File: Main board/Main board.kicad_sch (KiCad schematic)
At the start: 41 parts, among them J1 Conn_01x03

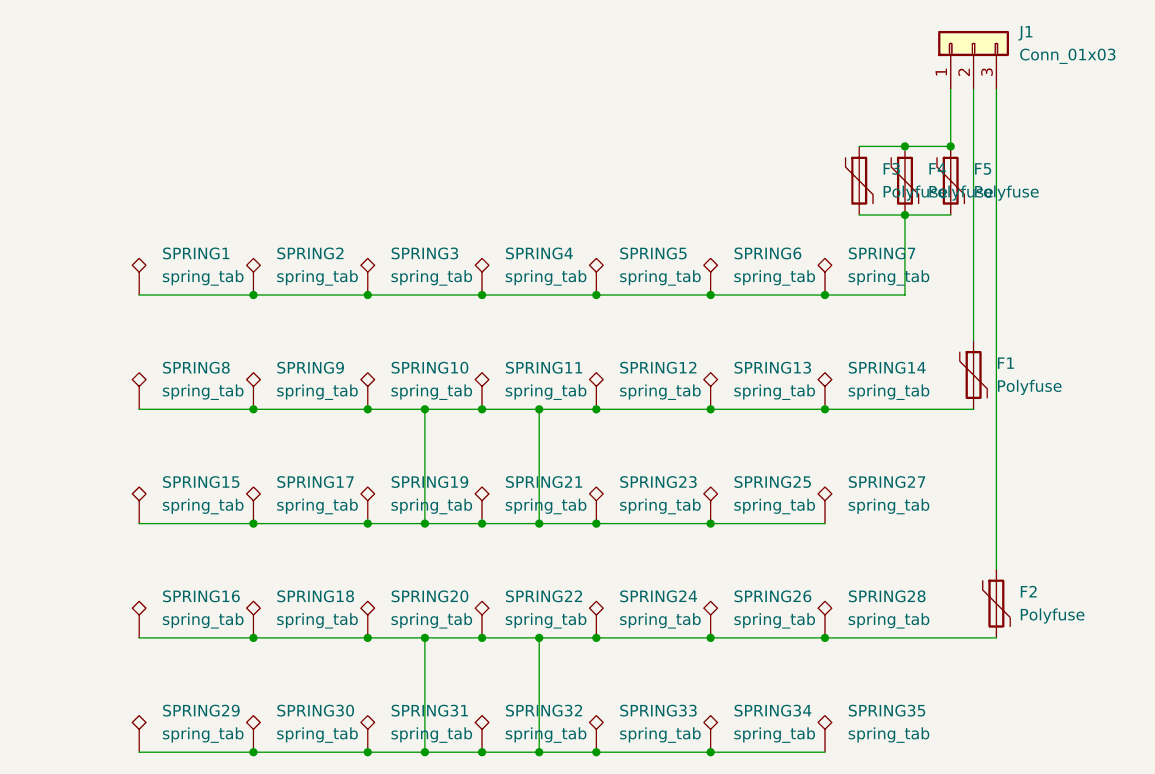
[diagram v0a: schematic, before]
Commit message: Created breakable symmetrical version
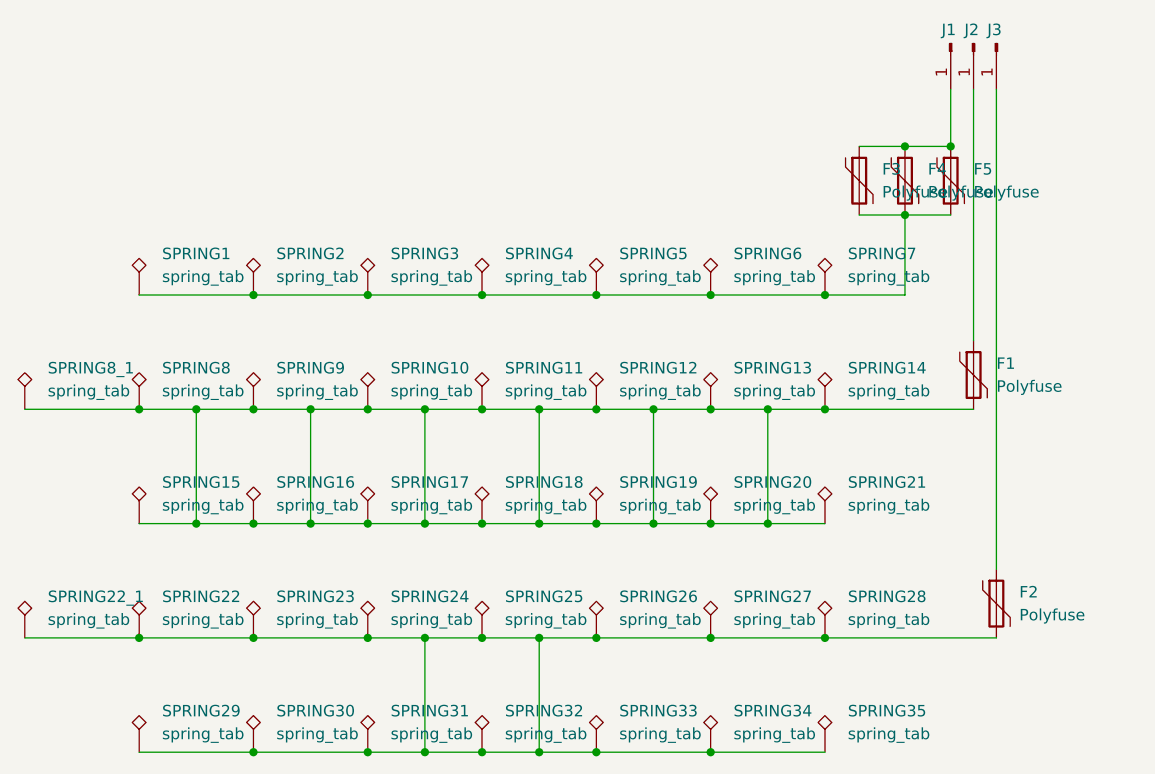
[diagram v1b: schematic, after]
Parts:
- removed J1: Conn_01x03, symbol Connector_Generic:Conn_01x03
- added J1, J2, J3: Conn_01x01_Pin, SMD_spring_clamp_connector:SMD_spring_clamp_connector_1x1, symbol Connector:Conn_01x01_Pin
- added SPRING22_1, SPRING8_1: spring_tab, spring_tab:spring_tab, symbol Connector:TestPoint_Alt
- F1, F2, F3, F4, F5: footprint (none) -> Fuse:Fuse_1812_4532Metric
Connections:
- net at F1.2, SPRING10.1, SPRING11.1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: now also SPRING16.1, SPRING18.1, SPRING20.1, SPRING8_1.1; no longer SPRING23.1, SPRING25.1, SPRING27.1
- net at F2.2, SPRING22.1, SPRING24.1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: now also SPRING23.1, SPRING25.1, SPRING27.1, SPRING22_1.1; no longer SPRING16.1, SPRING18.1, SPRING20.1
- net at F3.1, F4.1, F5.1: now also J1.1 (Pin_1)
- net at F2.1: now also J3.1 (Pin_1)
- net at F1.1: now also J2.1 (Pin_1)
